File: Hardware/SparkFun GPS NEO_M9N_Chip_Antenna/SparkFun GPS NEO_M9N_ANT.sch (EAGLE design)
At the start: 48 parts, among them J2 Qwiic Right Angle, J4 Qwiic Right Angle, U1 U-BLOX_NEO-M9N, U2 3.3V, Y1 GPS_CHIP_ANTENNAW3011

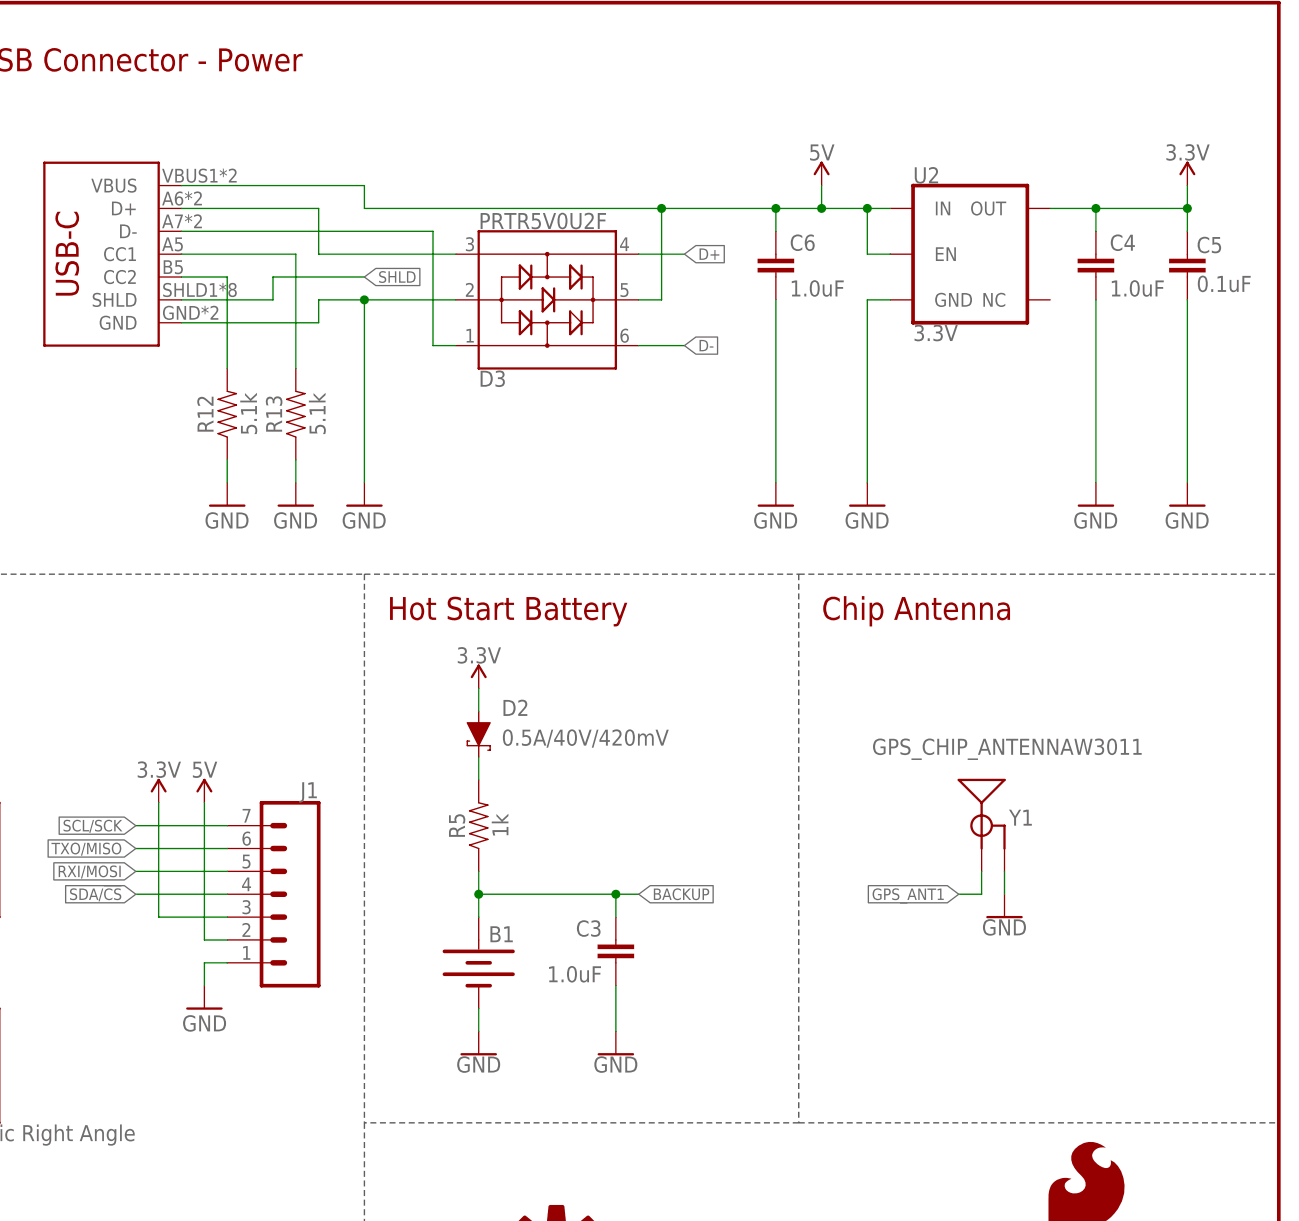
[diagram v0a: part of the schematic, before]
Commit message: Updates libs, adds SMA connector and rf bias circuit
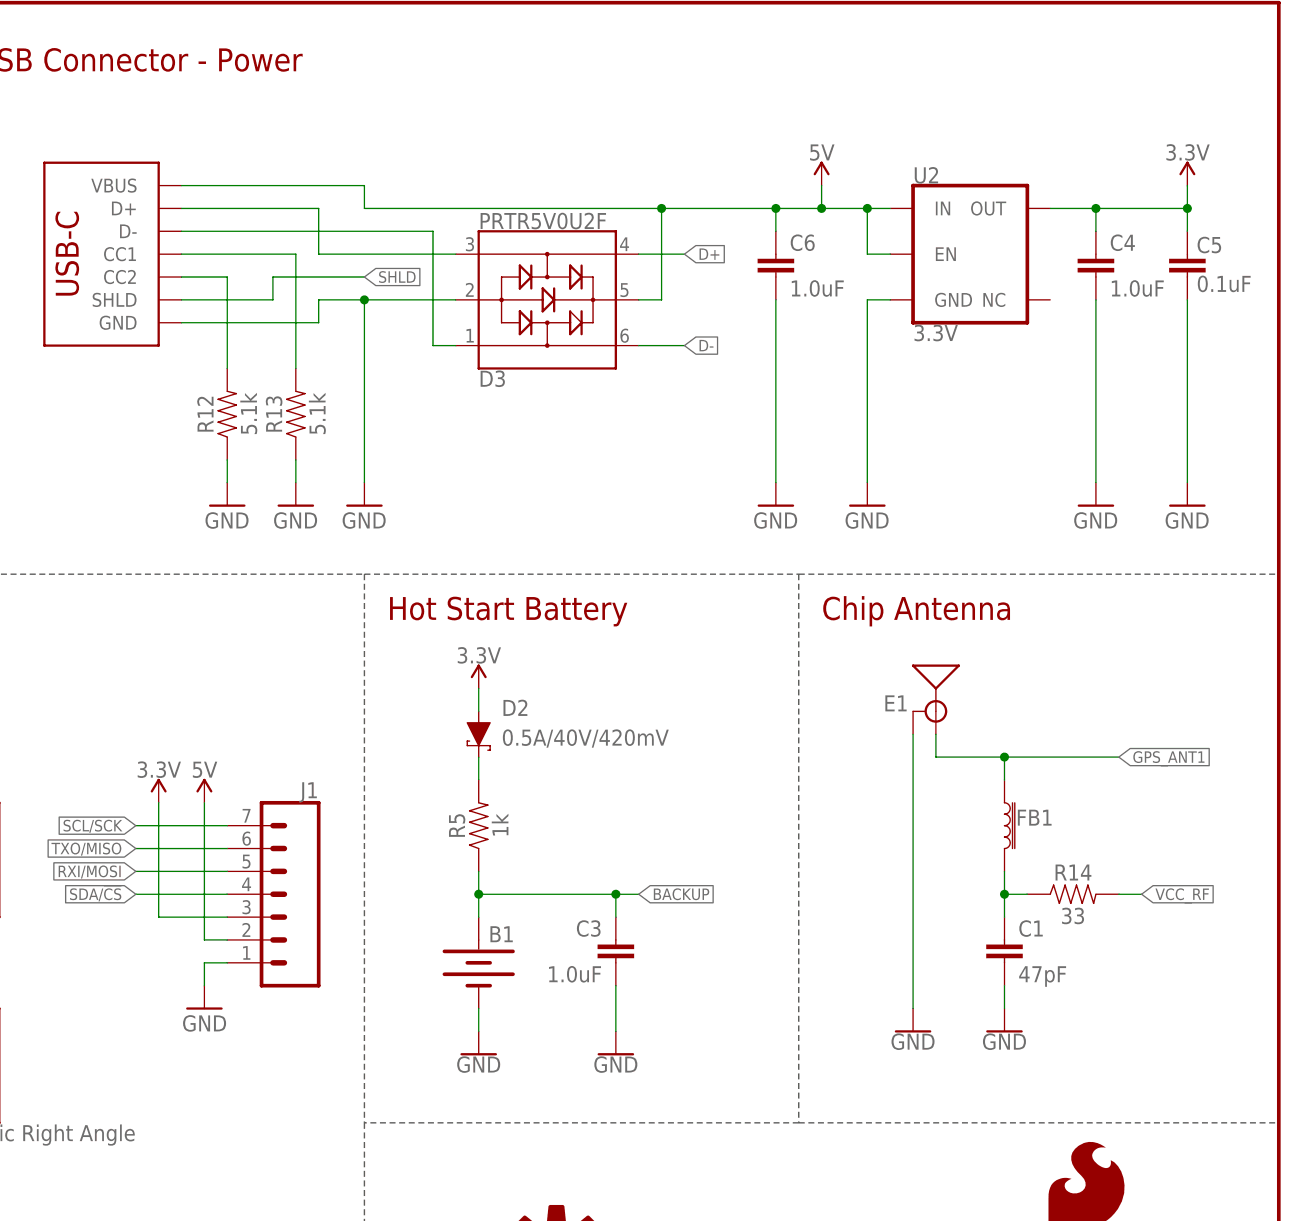
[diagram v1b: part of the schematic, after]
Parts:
- removed Y1: GPS_CHIP_ANTENNAW3011, SparkFun-GPS:GPS_CHIP_ANTENNAW3011
- added C1: 47pF, SparkFun-Capacitors:47PF-0402-25V-5%-X7R
- added E1: ANTENNA-GROUNDEDEDGE_RPSMA_SMD, SparkFun-RF:ANTENNA-GROUNDEDEDGE_RPSMA_SMD
- added FB1: FERRITE_BEAD-120_OHM-0402, SparkFun-Coils:FERRITE_BEAD-120_OHM-0402
- added R14: 33, SparkFun-Resistors:33OHM-0402-1/10W-1%
- J3: device SparkFun-Connectors:USB_C2-LAYER -> SparkFun-Connectors:USB_C_2-LAYER_PADS
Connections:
- new net N$3: C1.1, FB1.2, R14.1
- net GND: now also C1.2, E1.GND; no longer Y1.GND
- net GPS_ANT1: now also E1.SIGNAL, FB1.1; no longer Y1.SIGNAL
- net VCC_RF: now also R14.2
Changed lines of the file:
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@@
 <?xml version="1.0" encoding="utf-8"?>
 <!DOCTYPE eagle SYSTEM "eagle.dtd">
-<eagle version="9.5.1">
+<eagle version="9.5.2">
 <drawing>
 <settings>
@@
 <layer number="128" name="_bValues" color="7" fill="1" visible="yes" active="yes"/>
 <layer number="129" name="Mask" color="7" fill="1" visible="yes" active="yes"/>
+<layer number="130" name="SMDSTROOK" color="7" fill="1" visible="no" active="no"/>
 <layer number="131" name="tAdjust" color="7" fill="1" visible="yes" active="yes"/>
 <layer number="132" name="bAdjust" color="7" fill="1" visible="yes" active="yes"/>
+<layer number="133" name="bottom_silk" color="7" fill="1" visible="no" active="no"/>
+<layer number="134" name="silk_top" color="7" fill="1" visible="no" active="no"/>
+<layer number="135" name="silk_bottom" color="7" fill="1" visible="no" active="no"/>
+<layer number="136" name="silktop" color="7" fill="1" visible="no" active="no"/>
+<layer number="137" name="silkbottom" color="7" fill="1" visible="no" active="no"/>
+<layer number="138" name="EEE" color="7" fill="1" visible="no" active="no"/>
+<layer number="139" name="_tKeepout" color="7" fill="1" visible="no" active="no"/>
+<layer number="140" name="mbKeepout" color="7" fill="1" visible="no" active="no"/>
+<layer number="141" name="ASSEMBLY_TOP" color="7" fill="1" visible="no" active="no"/>
+<layer number="142" name="mbRestrict" color="7" fill="1" visible="no" active="no"/>
+<layer number="143" name="PLACE_BOUND_TOP" color="7" fill="1" visible="no" active="no"/>
 <layer number="144" name="Drill_legend" color="7" fill="1" visible="yes" active="yes"/>
+<layer number="145" name="DrillLegend_01-16" color="7" fill="1" visible="no" active="no"/>
+<layer number="146" name="DrillLegend_01-20" color="7" fill="1" visible="no" active="no"/>
+<layer number="147" name="PIN_NUMBER" color="7" fill="1" visible="no" active="no"/>
+<layer number="148" name="DrillLegend_01-20" color="7" fill="1" visible="no" active="no"/>
+<layer number="149" name="DrillLegend_02-15" color="7" fill="1" visible="no" active="no"/>
 <layer number="150" name="Notes" color="7" fill="1" visible="yes" active="yes"/>
 <layer number="151" name="HeatSink" color="7" fill="1" visible="yes" active="yes"/>
@@
 <layer number="154" name="FabDoc2" color="7" fill="1" visible="yes" active="yes"/>
 <layer number="155" name="FabDoc3" color="7" fill="1" visible="yes" active="yes"/>
+<layer number="166" name="AntennaArea" color="7" fill="1" visible="no" active="no"/>
+<layer number="168" name="4mmHeightArea" color="7" fill="1" visible="no" active="no"/>
+<layer number="191" name="mNets" color="7" fill="1" visible="no" active="no"/>
+<layer number="192" name="mBusses" color="7" fill="1" visible="no" active="no"/>
+<layer number="193" name="mPins" color="7" fill="1" visible="no" active="no"/>
+<layer number="194" name="mSymbols" color="7" fill="1" visible="no" active="no"/>
+<layer number="195" name="mNames" color="7" fill="1" visible="no" active="no"/>
+<layer number="196" name="mValues" color="7" fill="1" visible="no" active="no"/>
 <layer number="199" name="Contour" color="7" fill="1" visible="yes" active="yes"/>
 <layer number="200" name="200bmp" color="1" fill="10" visible="yes" active="yes"/>
@@
 <part name="D3" library="SparkFun-IC-Power" deviceset="PRTR5V0U2" device="F"/>
 <part name="J5" library="SparkFun-Connectors" deviceset="CONN_04" device="1X04_NO_SILK"/>
-<part name="J3" library="SparkFun-Connectors" deviceset="USB_C" device="2-LAYER"/>
+<part name="J3" library="SparkFun-Connectors" deviceset="USB_C" device="_2-LAYER_PADS"/>
 <part name="R12" library="SparkFun-Resistors" deviceset="5.1KOHM" device="5.1KOHM-0603-1/10W-1%" value="5.1k"/>
 <part name="R13" library="SparkFun-Resistors" deviceset="5.1KOHM" device="5.1KOHM-0603-1/10W-1%" value="5.1k"/>
@@
 <part name="R16" library="SparkFun-Resistors" deviceset="10KOHM" device="-0402-1/16W-1%" value="10k"/>
 <part name="SUPPLY12" library="SparkFun-PowerSymbols" deviceset="3.3V" device=""/>
-<part name="Y1" library="SparkFun-GPS" deviceset="GPS_CHIP_ANTENNA" device="W3011"/>
+<part name="E1" library="SparkFun-RF" deviceset="ANTENNA-GROUNDED" device="EDGE_RPSMA_SMD"/>
+<part name="FB1" library="SparkFun-Coils" deviceset="FERRITE_BEAD-120_OHM" device="-0402"/>
+<part name="C1" library="SparkFun-Capacitors" deviceset="47PF" device="-0402-25V-5%-X7R" value="47pF"/>
+<part name="R14" library="SparkFun-Resistors" deviceset="33OHM" device="-0402-1/10W-1%" value="33"/>
+<part name="GND2" library="SparkFun-PowerSymbols" deviceset="GND" device=""/>
 </parts>
 <sheets>
@@
 <attribute name="VALUE" x="129.54" y="127" size="1.778" layer="96" font="vector"/>
 </instance>
-<instance part="GND27" gate="1" x="218.44" y="83.82" smashed="yes">
-<attribute name="VALUE" x="218.44" y="83.566" size="1.778" layer="96" font="vector" align="top-center"/>
+<instance part="GND27" gate="1" x="208.28" y="71.12" smashed="yes">
+<attribute name="VALUE" x="208.28" y="70.866" size="1.778" layer="96" font="vector" align="top-center"/>
 </instance>
 <instance part="C4" gate="G$1" x="228.6" y="154.94" smashed="yes">
@@
 <attribute name="VALUE" x="17.78" y="40.894" size="1.778" layer="96" font="vector" align="bottom-center"/>
 </instance>
-<instance part="Y1" gate="G$1" x="215.9" y="99.06" smashed="yes">
-<attribute name="NAME" x="218.948" y="93.98" size="1.778" layer="95" font="vector"/>
-<attribute name="VALUE" x="203.708" y="101.854" size="1.778" layer="96" font="vector"/>
+<instance part="E1" gate="G$1" x="210.82" y="106.68" smashed="yes" rot="MR0">
+<attribute name="NAME" x="207.772" y="106.68" size="1.778" layer="95" font="vector" rot="MR0"/>
+</instance>
+<instance part="FB1" gate="G$1" x="218.44" y="93.98" smashed="yes">
+<attribute name="NAME" x="219.71" y="93.98" size="1.778" layer="95" font="vector"/>
+</instance>
+<instance part="C1" gate="G$1" x="218.44" y="78.74" smashed="yes">
+<attribute name="NAME" x="219.964" y="81.661" size="1.778" layer="95" font="vector"/>
+<attribute name="VALUE" x="219.964" y="76.581" size="1.778" layer="96" font="vector"/>
+</instance>
+<instance part="R14" gate="G$1" x="226.06" y="86.36" smashed="yes">
+<attribute name="NAME" x="226.06" y="87.884" size="1.778" layer="95" font="vector" align="bottom-center"/>
+<attribute name="VALUE" x="226.06" y="84.836" size="1.778" layer="96" font="vector" align="top-center"/>
+</instance>
+<instance part="GND2" gate="1" x="218.44" y="71.12" smashed="yes">
+<attribute name="VALUE" x="218.44" y="70.866" size="1.778" layer="96" font="vector" align="top-center"/>
 </instance>
 </instances>
@@
 </segment>
 <segment>
-<pinref part="Y1" gate="G$1" pin="GND"/>
-<wire x1="218.44" y1="88.9" x2="218.44" y2="86.36" width="0.1524" layer="91"/>
 <pinref part="GND27" gate="1" pin="GND"/>
+<pinref part="E1" gate="G$1" pin="GND"/>
+<wire x1="208.28" y1="104.14" x2="208.28" y2="73.66" width="0.1524" layer="91"/>
+</segment>
+<segment>
+<pinref part="C1" gate="G$1" pin="2"/>
+<wire x1="218.44" y1="76.2" x2="218.44" y2="73.66" width="0.1524" layer="91"/>
+<pinref part="GND2" gate="1" pin="GND"/>
 </segment>
 </net>
@@
 <net name="GPS_ANT1" class="3">
 <segment>
-<label x="213.36" y="86.36" size="1.27" layer="95" rot="R180" xref="yes"/>
-<wire x1="215.9" y1="86.36" x2="213.36" y2="86.36" width="0.1524" layer="91"/>
-<wire x1="215.9" y1="86.36" x2="215.9" y2="88.9" width="0.1524" layer="91"/>
-<pinref part="Y1" gate="G$1" pin="SIGNAL"/>
+<label x="231.14" y="101.6" size="1.27" layer="95" xref="yes"/>
+<pinref part="E1" gate="G$1" pin="SIGNAL"/>
+<wire x1="210.82" y1="104.14" x2="210.82" y2="101.6" width="0.1524" layer="91"/>
+<wire x1="210.82" y1="101.6" x2="218.44" y2="101.6" width="0.1524" layer="91"/>
+<pinref part="FB1" gate="G$1" pin="1"/>
+<wire x1="218.44" y1="101.6" x2="231.14" y2="101.6" width="0.1524" layer="91"/>
+<wire x1="218.44" y1="99.06" x2="218.44" y2="101.6" width="0.1524" layer="91"/>
+<junction x="218.44" y="101.6"/>
 </segment>
 <segment>
@@
 <label x="20.32" y="149.86" size="1.27" layer="95" rot="R180" xref="yes"/>
 </segment>
+<segment>
+<pinref part="R14" gate="G$1" pin="2"/>
+<wire x1="231.14" y1="86.36" x2="233.68" y2="86.36" width="0.1524" layer="91"/>
+<label x="233.68" y="86.36" size="1.27" layer="95" font="vector" xref="yes"/>
+</segment>
 </net>
 <net name="D+" class="0">
@@
 </segment>
 </net>
+<net name="N$3" class="0">
+<segment>
+<pinref part="C1" gate="G$1" pin="1"/>
+<pinref part="FB1" gate="G$1" pin="2"/>
+<wire x1="218.44" y1="83.82" x2="218.44" y2="86.36" width="0.1524" layer="91"/>
+<pinref part="R14" gate="G$1" pin="1"/>
+<wire x1="218.44" y1="86.36" x2="218.44" y2="88.9" width="0.1524" layer="91"/>
+<wire x1="220.98" y1="86.36" x2="218.44" y2="86.36" width="0.1524" layer="91"/>
+<junction x="218.44" y="86.36"/>
+</segment>
+</net>

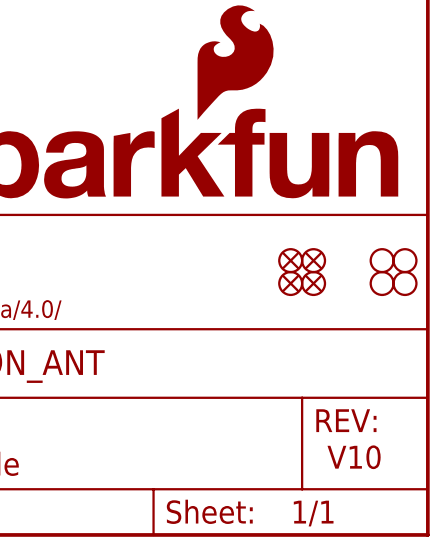
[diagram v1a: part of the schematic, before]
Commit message: Routed updates USB footprint and SMA connector with its RF circuitry
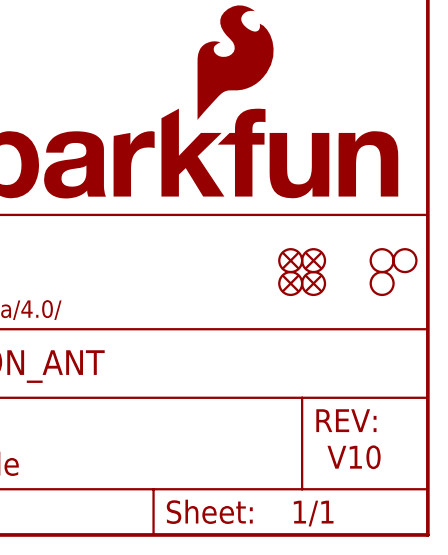
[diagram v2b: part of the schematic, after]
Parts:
- removed JP41: STAND-OFF, SparkFun:STAND-OFF
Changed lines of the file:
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@@
 <parts>
 <part name="JP31" library="SparkFun" deviceset="STAND-OFF" device=""/>
-<part name="JP41" library="SparkFun" deviceset="STAND-OFF" device=""/>
 <part name="JP21" library="SparkFun" deviceset="FIDUCIAL" device="UFIDUCIAL"/>
 <part name="JP61" library="SparkFun" deviceset="FIDUCIAL" device="UFIDUCIAL"/>
@@
 <instances>
 <instance part="JP31" gate="G$1" x="246.38" y="30.48" smashed="yes"/>
-<instance part="JP41" gate="G$1" x="246.38" y="27.94" smashed="yes"/>
 <instance part="JP21" gate="G$1" x="233.68" y="30.48" smashed="yes" rot="R270"/>
 <instance part="JP61" gate="G$1" x="236.22" y="30.48" smashed="yes"/>
